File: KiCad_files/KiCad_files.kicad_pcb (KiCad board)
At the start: 2 copper layers, 82 x 102 mm, 74 parts, among them J1 Conn_01x02_Socket, J2 L717HDE15P, J3 Conn_01x03_Socket, SW1 WE430182070816, U1 LM22670QMR-5.0, U2 MC33275ST-3.3T3G, U3 ADM3488ExR, U6 LT1789

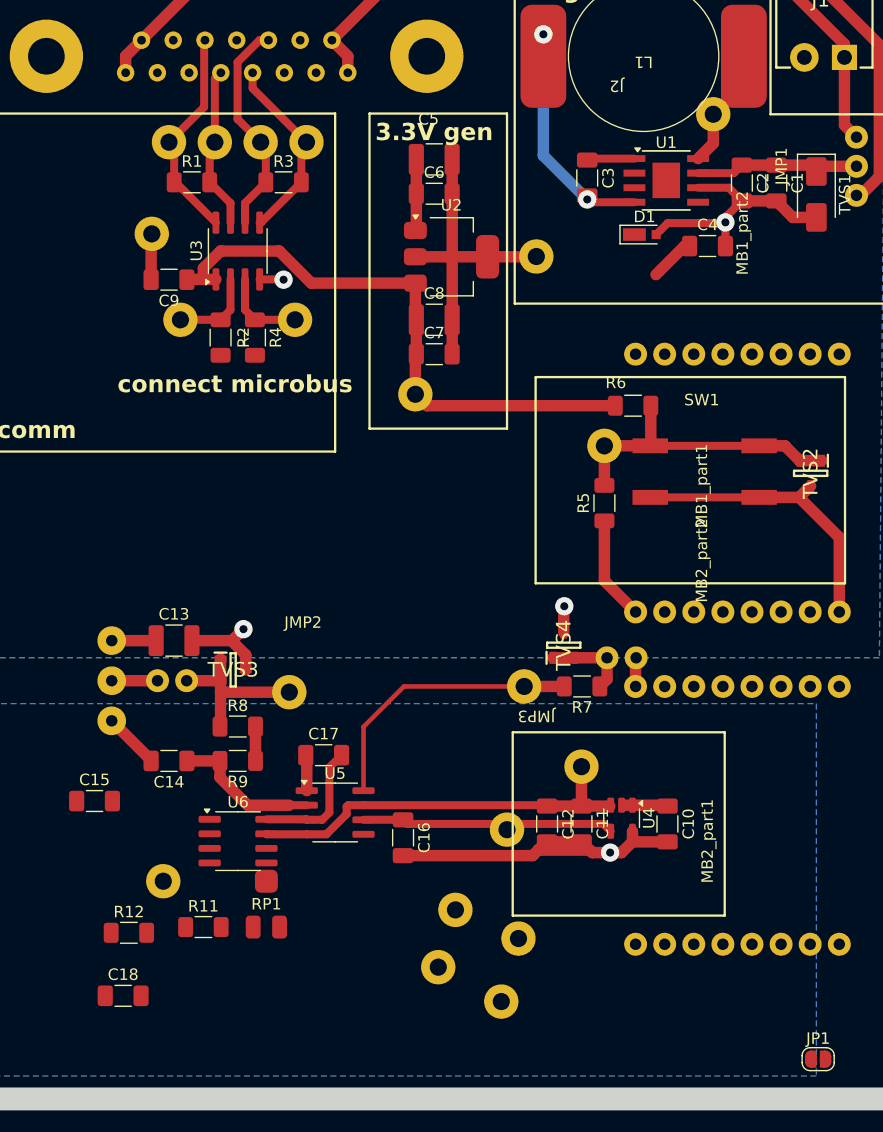
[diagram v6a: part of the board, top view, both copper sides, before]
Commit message: placed components and drew lines
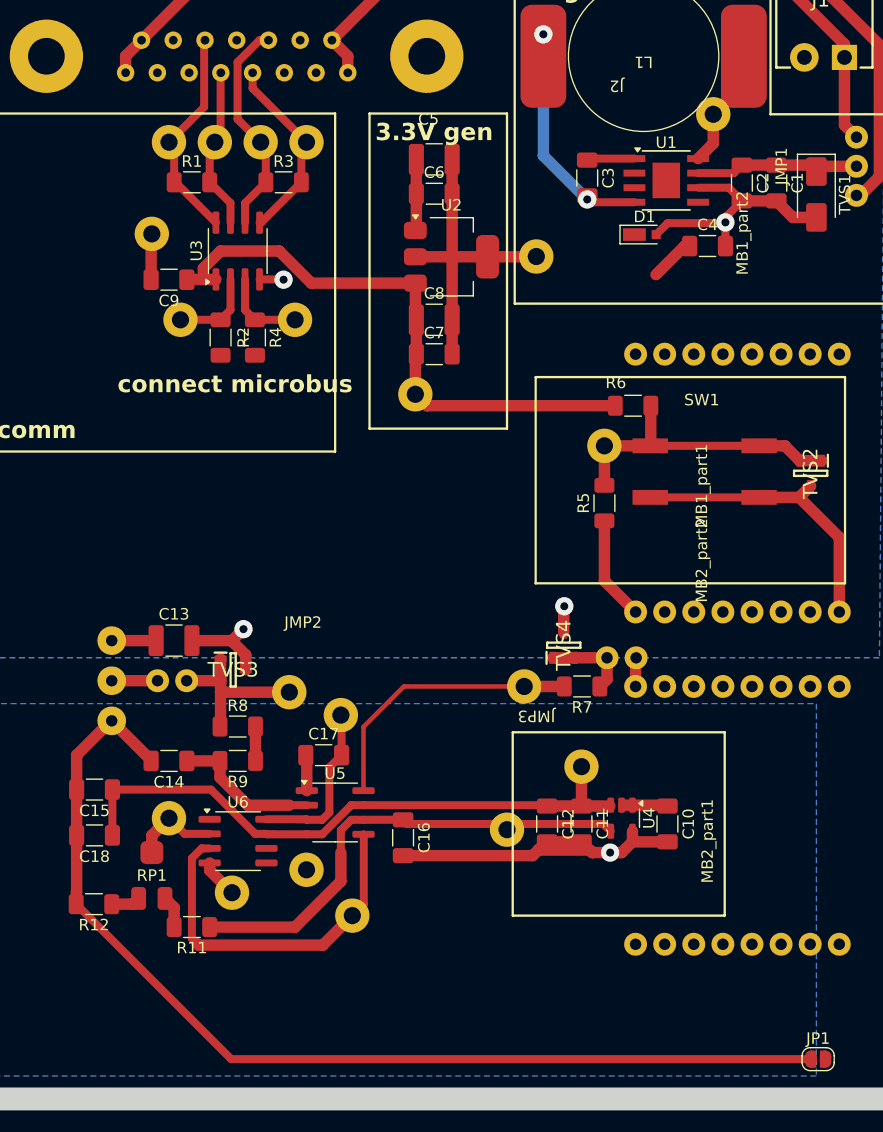
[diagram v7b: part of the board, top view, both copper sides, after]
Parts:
- moved TP15 26.9 mm to (136.5, 116.5)
- moved TGA1 25.3 mm to (142.0, 123.0)
- moved TP16 24.9 mm to (151.5, 107.5)
- moved TP14 16.8 mm to (152.5, 125.0)
- moved C18 14.2 mm to (130.0, 118.0), turned to 180 degrees
- moved TP17 13.5 mm to (148.5, 121.0)
- moved RP1 10.3 mm to (135.0, 121.5)
- moved R12 3.94 mm to (129.9, 124.0), turned to 180 degrees
- moved C15 1.00 mm to (130.0, 114.0), turned to 180 degrees
- moved R11 1.00 mm to (138.5, 126.0), turned to 180 degrees
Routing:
- net GNDA: track 46.2 -> 139.5 mm
- net Net-(U5-out): track 0.00 -> 31.7 mm
- net /VBIAS: track 22.0 -> 41.9 mm
- net +3.3VA: track 34.9 -> 53.5 mm
- net Net-(RP1-WIPER): track 0.00 -> 7.74 mm
- net Net-(RP1-CCW): track 0.00 -> 2.83 mm
- net Net-(RP1-CW): track 0.00 -> 2.56 mm

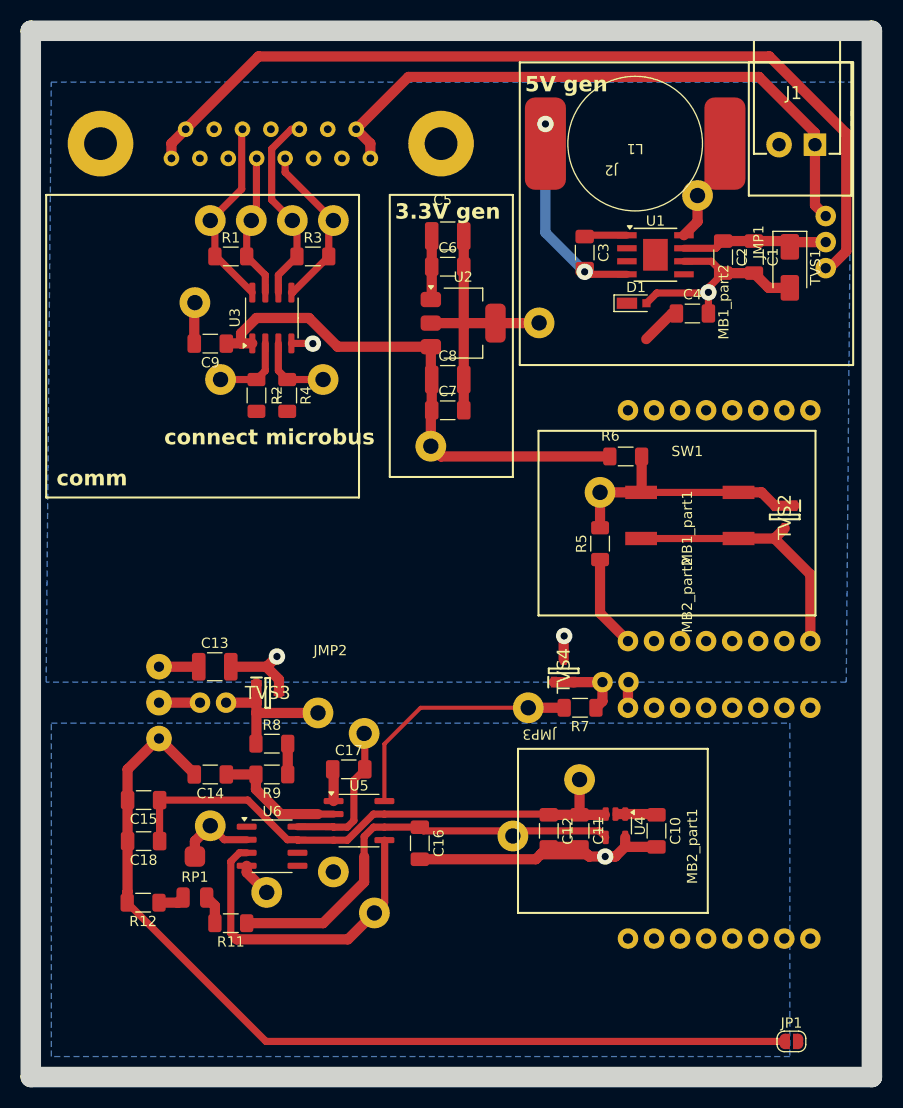
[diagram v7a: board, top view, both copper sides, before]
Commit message: Completed first version of the PCB
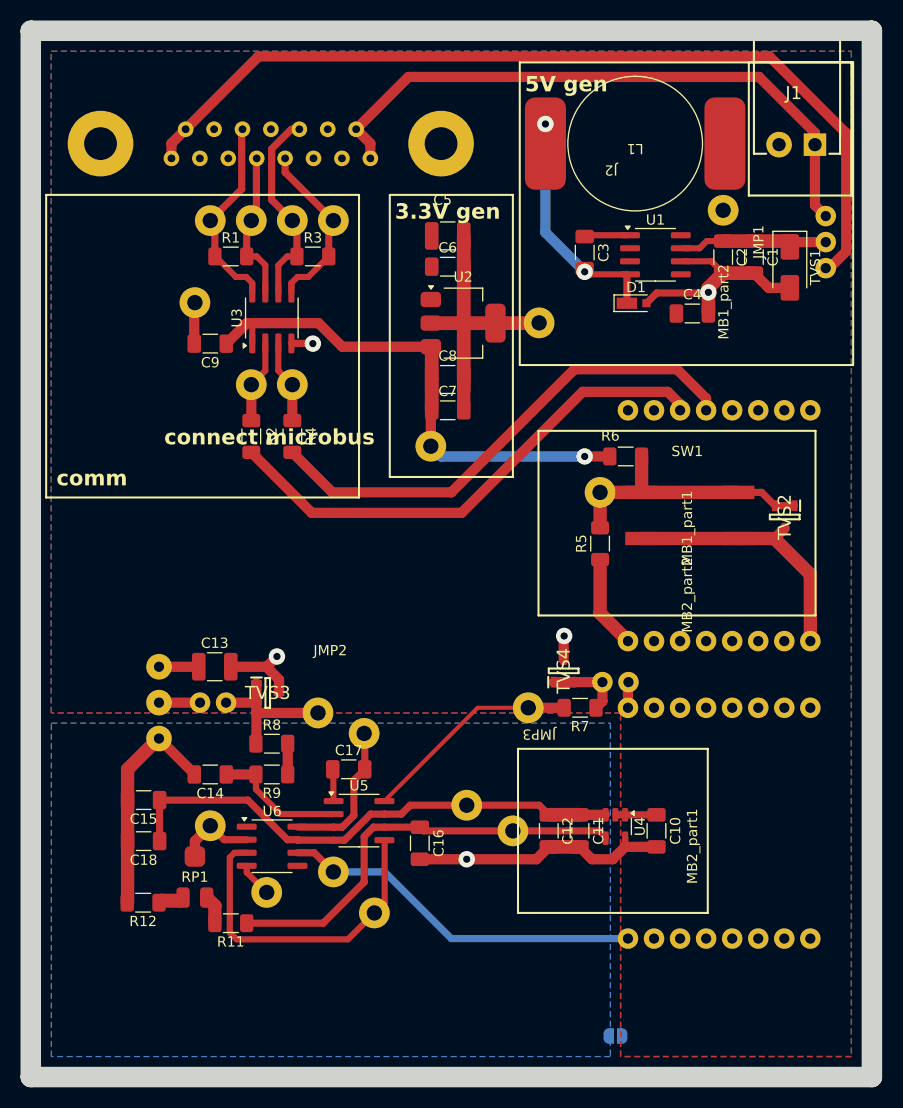
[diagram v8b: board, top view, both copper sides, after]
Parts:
- JP1: moved to B.Cu
- U1: footprint Package_SO:TI_SO-PowerPAD-8 -> Package_SO:SOIC-8_3.9x4.9mm_P1.27mm
- moved JP1 17.2 mm to (176.0, 137.0)
- moved TP10 11.3 mm to (161.5, 114.5)
- moved R2 4.03 mm to (140.5, 78.5)
- moved R4 4.03 mm to (144.5, 78.5)
- moved TP5 3.04 mm to (140.5, 73.5)
- moved TP8 3.04 mm to (144.5, 73.5)
- moved TP1 2.88 mm to (186.5, 56.5)
- moved TP11 0.50 mm to (166.0, 117.0)
- moved U4 0.07 mm to (176.0, 116.6)
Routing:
- net GNDA: track 139.5 -> 65.9 mm
- net /MB1_14: track 0.00 -> 50.2 mm
- net /MB1_13: track 0.00 -> 49.3 mm
- net /MB2_1: track 0.00 -> 35.7 mm
- net +5V: track 30.4 -> 12.5 mm
- net Net-(U5-clk): track 24.6 -> 21.3 mm
- net Net-(D1-K): track 20.3 -> 23.2 mm
- net +3.3VA: track 53.5 -> 50.8 mm
- net GNDD: track 92.9 -> 94.4 mm
- net Net-(RP1-CW): track 2.56 -> 1.79 mm
- net /13: track 19.0 -> 19.7 mm
- net /5: track 14.2 -> 14.8 mm
- net /11: track 19.3 -> 19.8 mm
- net /4: track 16.8 -> 17.3 mm
- net +3.3V: track 51.4 -> 51.2 mm, vias 0 -> 1
- added copper zone on F.Cu, net +5V
